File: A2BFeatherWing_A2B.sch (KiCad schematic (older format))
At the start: 13 parts, among them U2 AD2428W

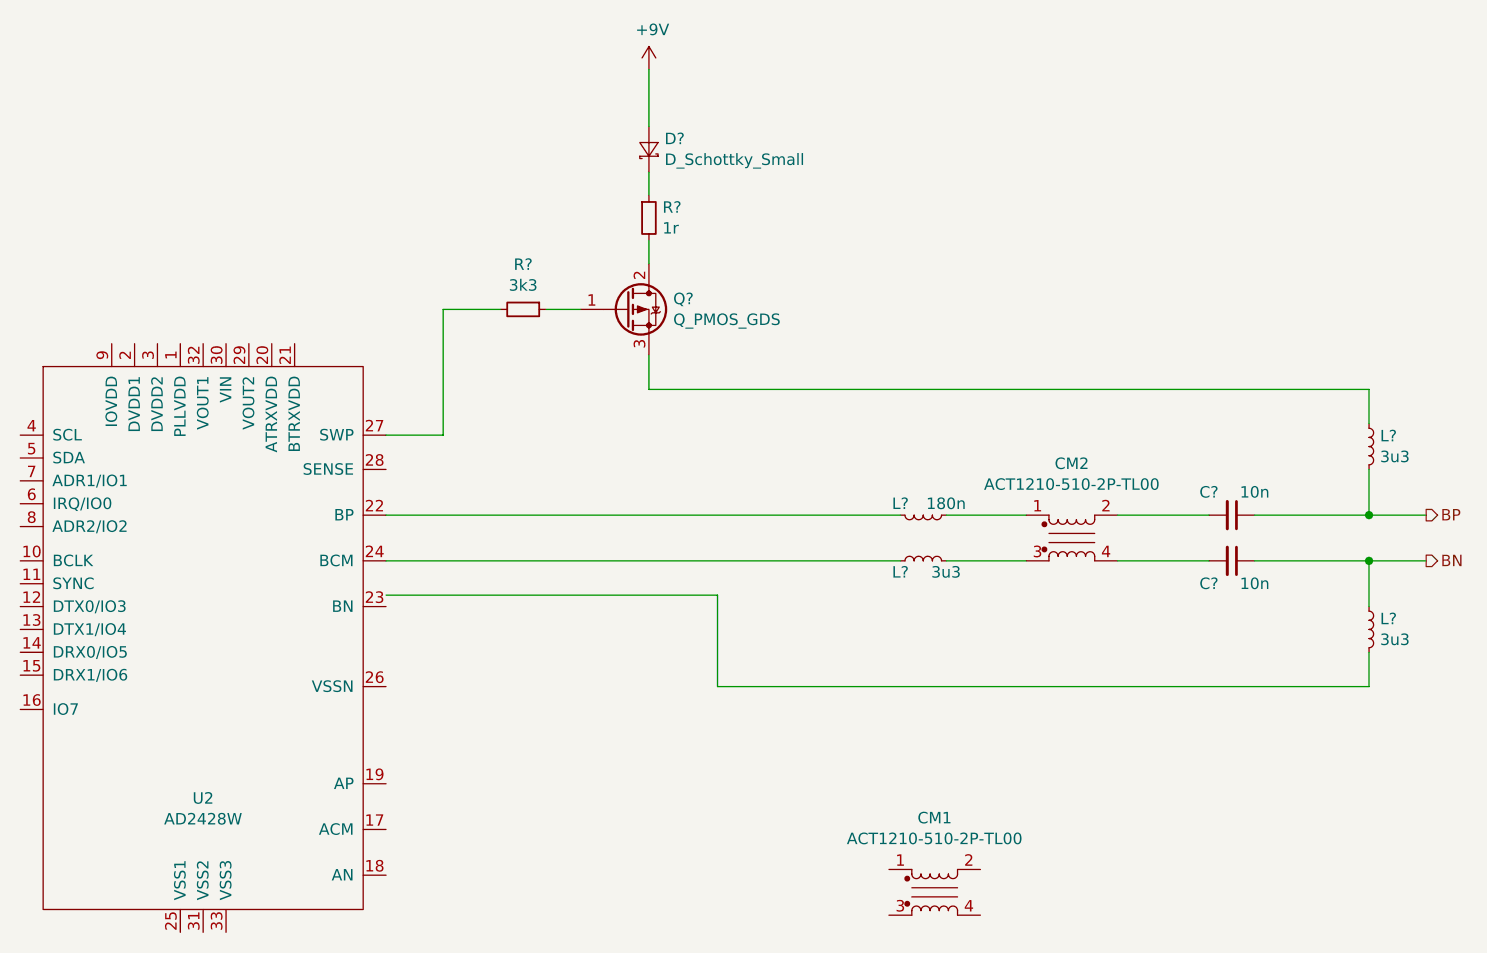
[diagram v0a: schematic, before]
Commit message: generate BOM, update some footprints
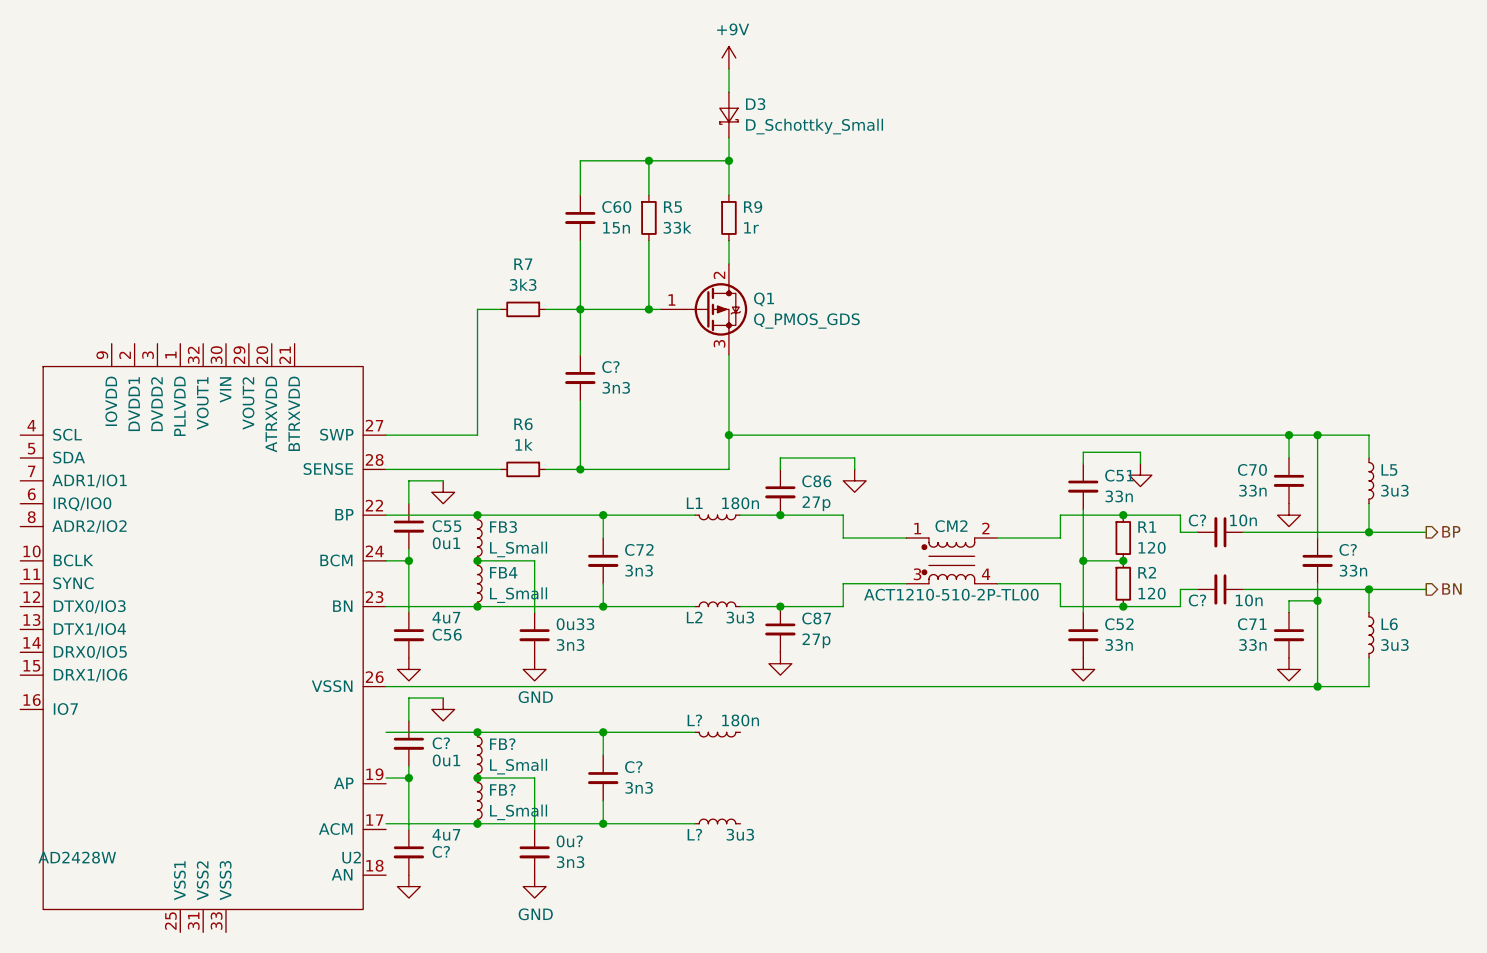
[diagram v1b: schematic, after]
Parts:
- removed CM1: ACT1210-510-2P-TL00, Knochi_Filters:CommonModeChoke_TDK_ACT1210, symbol Knochi_Inductors:ACT1210-510-2P-TL00
- added 0u33, 0u?, C72, C? (x2): 3n3, symbol Device:C_Small
- added C51, C52, C70, C71, C?: 33n, symbol Device:C_Small
- added C55, C?: 0u1, symbol Device:C_Small
- added C56, C?: 4u7, symbol Device:C_Small
- added C60: 15n, symbol Device:C_Small
- added C86, C87: 27p, symbol Device:C_Small
- added FB3, FB4, FB? (x2): L_Small, symbol Device:L_Small
- added L?: 180n, symbol Device:L_Small
- added L?: 3u3, symbol Device:L_Small
- added R1, R2: 120, symbol Device:R_Small
- added R5: 33k, symbol Device:R_Small
- added R6: 1k, symbol Device:R_Small
- gave numbers to parts that had none: 8
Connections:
- net labels added: GND
- wire segments 26 -> 101
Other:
- moved on the sheet: C?, CM2, D3, L1, L2, L5, L6, Q1, R9

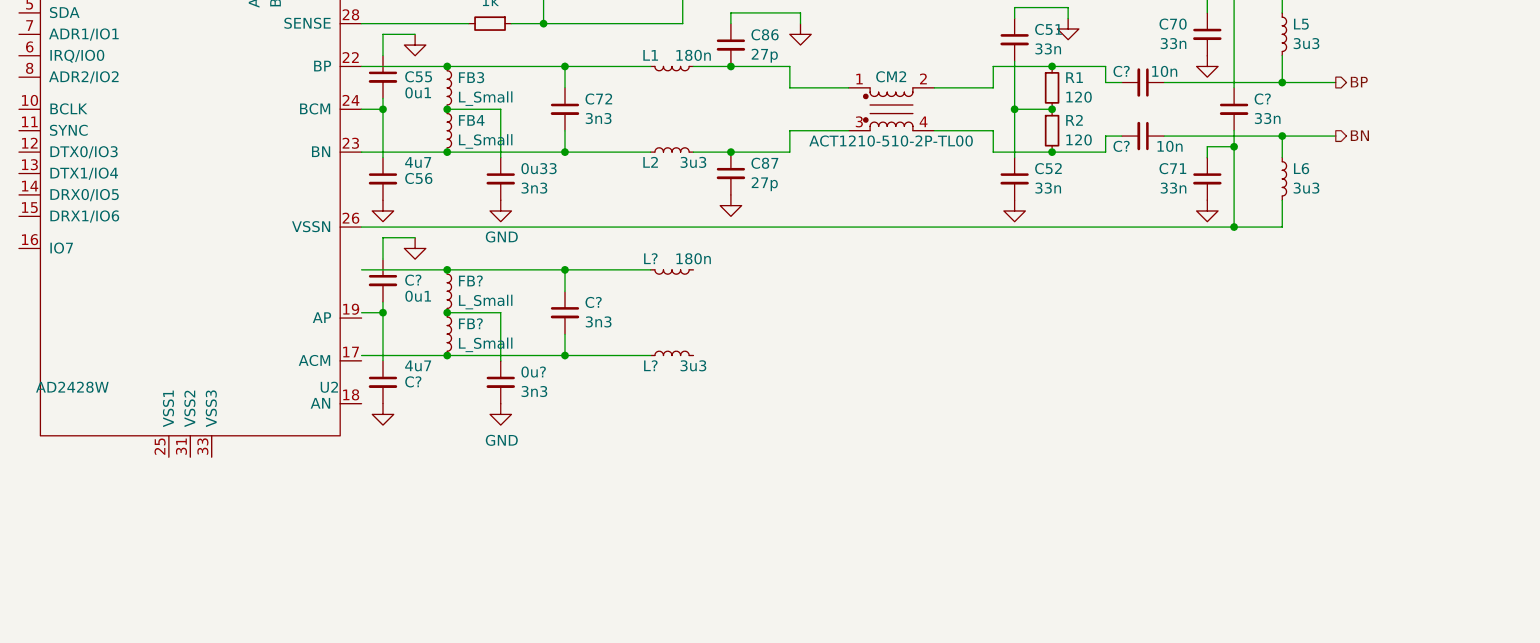
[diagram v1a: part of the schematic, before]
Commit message: local powered slave filtnet
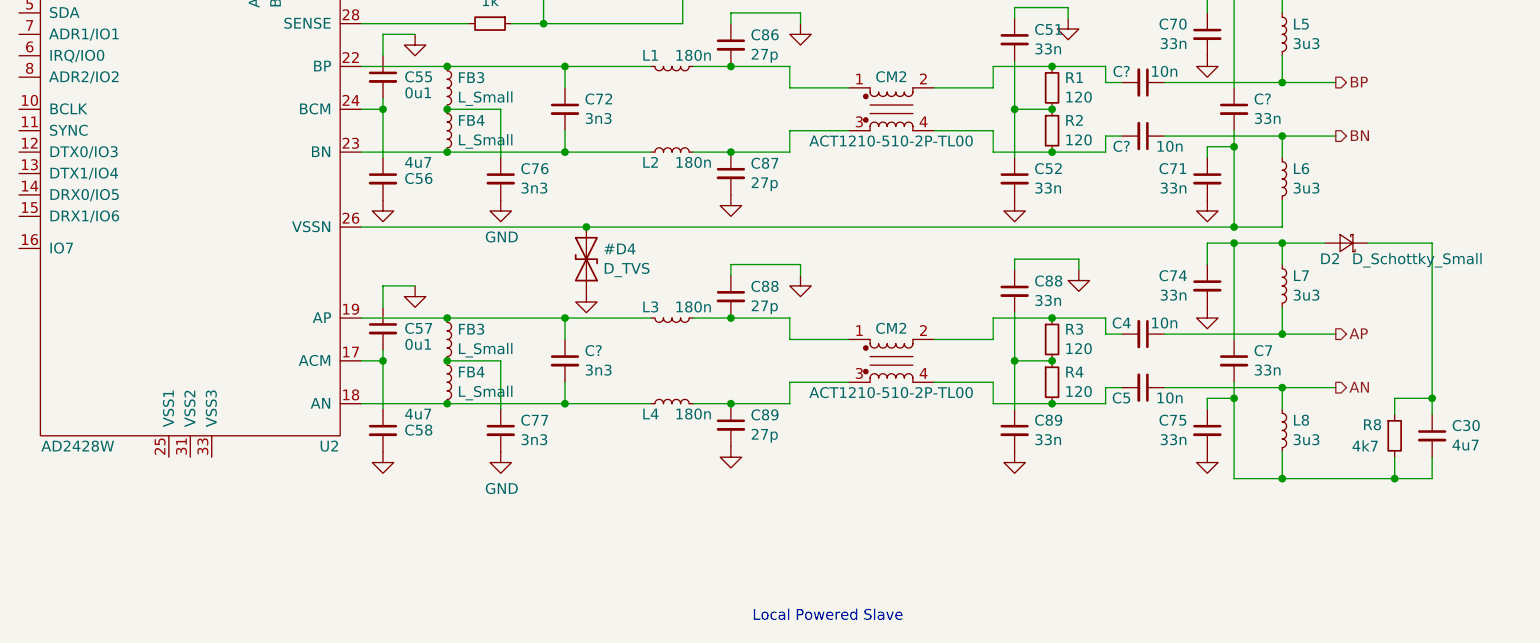
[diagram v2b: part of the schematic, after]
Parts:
- added C30: 4u7, symbol Device:C_Small
- added C4, C5: 10n, symbol Device:C_Small
- added C7, C74, C75, C88, C89: 33n, symbol Device:C_Small
- added C88, C89: 27p, symbol Device:C_Small
- added CM2: ACT1210-510-2P-TL00, Knochi_Filters:CommonModeChoke_TDK_ACT1210, symbol Knochi_Inductors:ACT1210-510-2P-TL00
- added D2: D_Schottky_Small, symbol Device:D_Schottky_Small
- added L7, L8: 3u3, symbol Device:L_Small
- added R3, R4: 120, symbol Device:R_Small
- added R8: 4k7, symbol Device:R_Small
- L2: value 3u3 -> 180n
- L4: renamed from L?; value 3u3 -> 180n
- gave numbers to parts that had none: 6
- renumbered 0u33 to C76
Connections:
- net labels added: AN, AP, D_TVS
- wire segments 101 -> 158
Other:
- note added: "Local Powered Slave"
- moved on the sheet: C57, C58, C77, C?, FB3, FB4, L3, L4

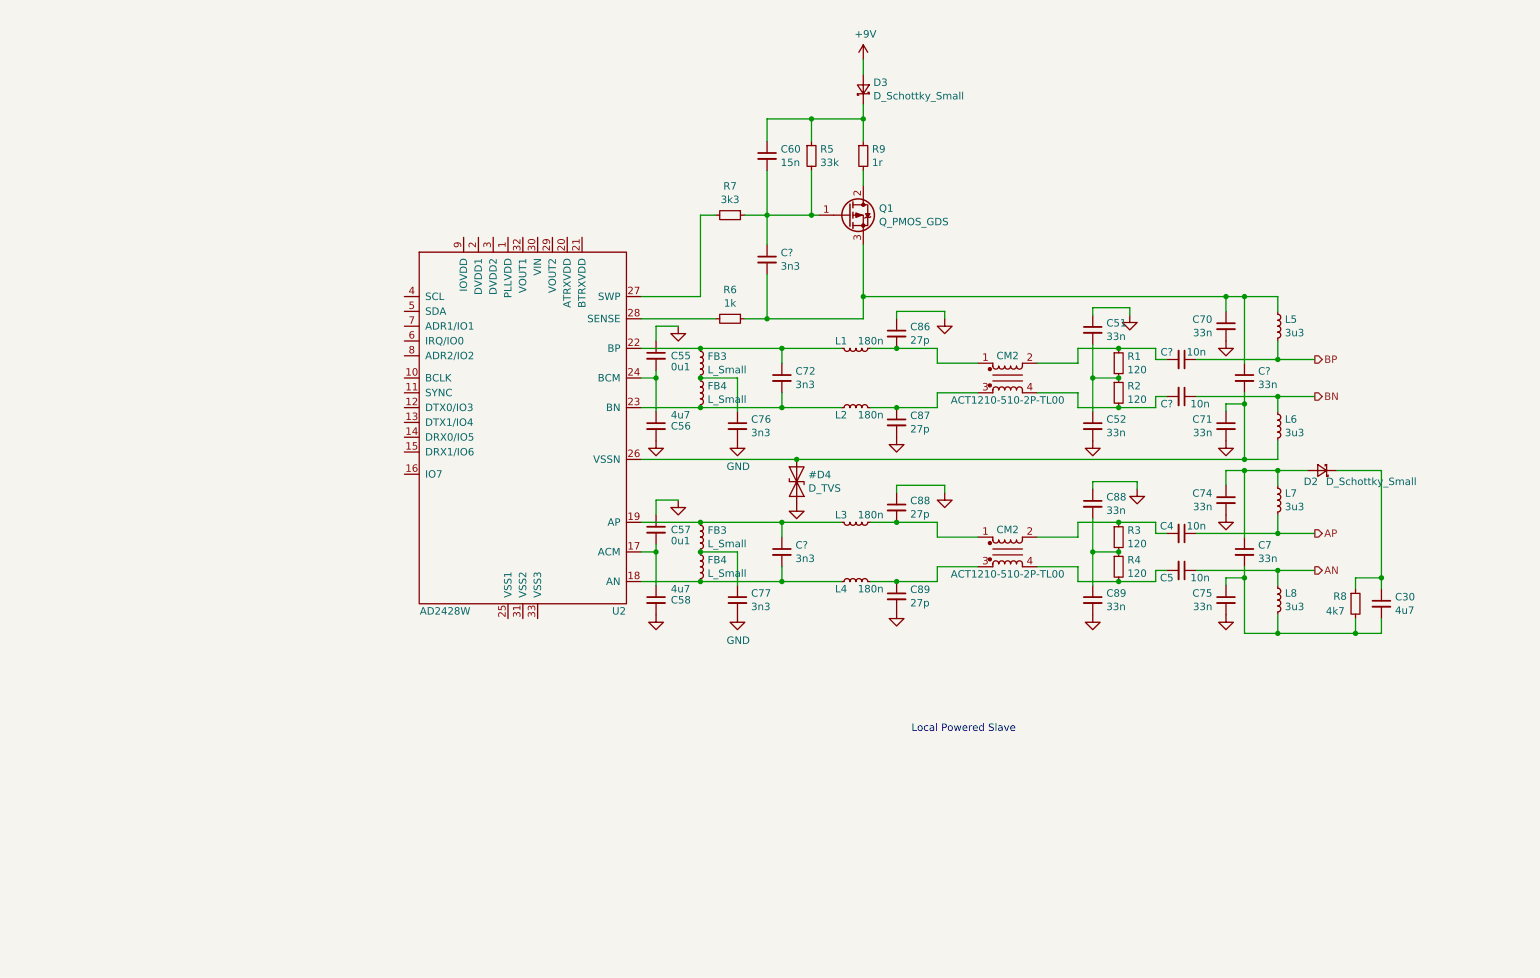
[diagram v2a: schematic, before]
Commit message: added datasheets, power
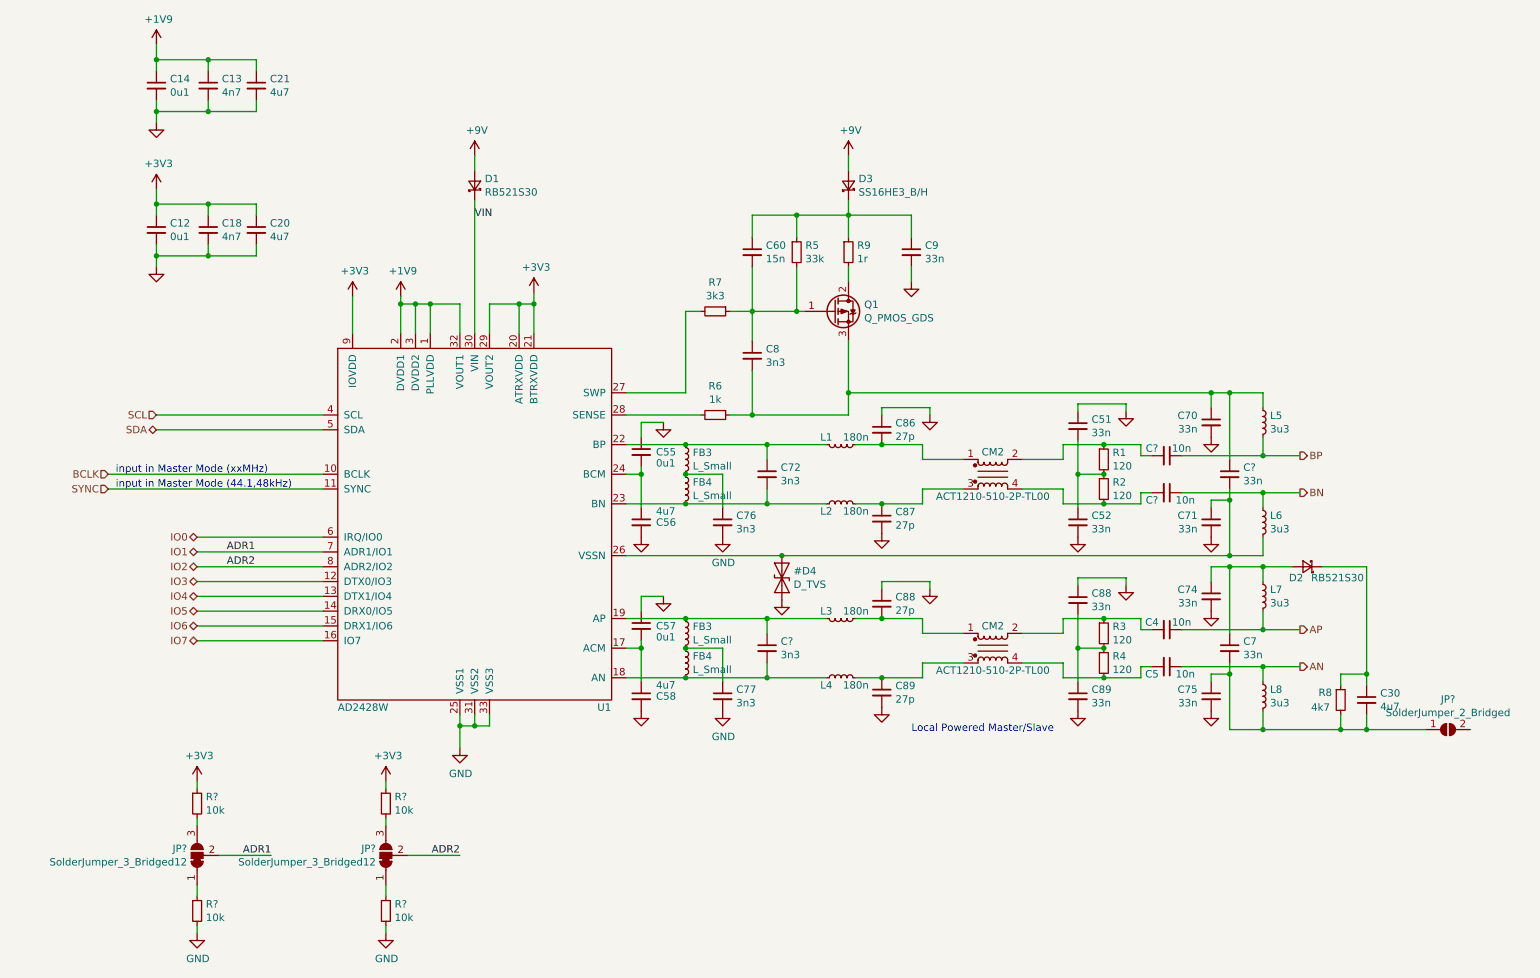
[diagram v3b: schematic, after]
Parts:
- removed U2: AD2428W, Package_DFN_QFN:QFN-32-1EP_5x5mm_P0.5mm_EP3.6x3.6mm, symbol Knochi_Transceivers:AD2428W
- added C12, C14: 0u1, symbol Device:C_Small
- added C13, C18: 4n7, symbol Device:C_Small
- added C20, C21: 4u7, symbol Device:C_Small
- added C9: 33n, symbol Device:C_Small
- added D1: RB521S30, symbol Device:D_Schottky_Small
- added JP?: SolderJumper_2_Bridged, symbol Jumper:SolderJumper_2_Open
- added JP? (x2): SolderJumper_3_Bridged12, symbol Jumper:SolderJumper_3_Bridged12
- added R? (x4): 10k, symbol Device:R_Small
- added U1: AD2428W, Package_DFN_QFN:QFN-32-1EP_5x5mm_P0.5mm_EP3.6x3.6mm, symbol A2BFeatherWing:AD2428W-Knochi_Transceivers
- D2: value D_Schottky_Small -> RB521S30
- D3: value D_Schottky_Small -> SS16HE3_B/H
- gave numbers to parts that had none: 1
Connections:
- net +9V: now also D1.2 (A)
- net GND: now also C12.2, C13.2, C14.2, C18.2, C20.2, C21.2, C9.2, R?.2, R?.2, U1.25 (VSS1), U1.31 (VSS2), U1.33 (VSS3)
- net at C57.2, C58.1: now also U1.17 (ACM)
- net at C?.2, FB4.2, L4.1: now also U1.18 (AN)
- net at C?.1, FB3.1, L3.2: now also U1.19 (AP)
- net at C72.1, FB3.1, L1.2: now also U1.22 (BP)
- net at C72.2, FB4.2, L2.1: now also U1.23 (BN)
- net at C55.2, C56.1: now also U1.24 (BCM)
- net at C71.1, C?.2, L6.2: now also U1.26 (VSSN)
- net at R7.2: now also U1.27 (SWP)
- net at R6.2: now also U1.28 (SENSE)
- net at C60.1, D3.1 (K), R5.1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: now also C9.1
- net at C30.2, C7.2, C75.1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: now also JP?.1 (A)
- new net: JP?.1 (A), R?.1 (x2)
- new net: JP?.3 (B), R?.2 (x2)
- new net +1V9: C13.1, C14.1, C21.1, U1.1 (PLLVDD), U1.2 (DVDD1), U1.3 (DVDD2), U1.32 (VOUT1)
- new net +3V3: C12.1, C18.1, C20.1, R?.1, R?.1, U1.20 (ATRXVDD), U1.21 (BTRXVDD), U1.29 (VOUT2), U1.9 (IOVDD)
- new net BCLK: U1.10 (BCLK)
- new net IO0: U1.6 (IRQ/IO0)
- new net IO1: JP?.2 (C), U1.7 (ADR1/IO1)
- new net IO2: JP?.2 (C), U1.8 (ADR2/IO2)
- new net IO3: U1.12 (DTX0/IO3)
- new net IO4: U1.13 (DTX1/IO4)
- new net IO5: U1.14 (DRX0/IO5)
- new net IO6: U1.15 (DRX1/IO6)
- new net IO7: U1.16 (IO7)
- new net SCL: U1.4 (SCL)
- new net SDA: U1.5 (SDA)
- new net SYNC: U1.11 (SYNC)
- new net VIN: D1.1 (K), U1.30 (VIN)
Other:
- note added: "Local Powered Master/Slave"
- note added: "input in Master Mode (44.1,48kHz)"
- note added: "input in Master Mode (xxMHz)"
- note removed: "Local Powered Slave"
- moved on the sheet: C30, C4, C5, C51, C52, C55, C56, C57, C58, C60, C7, C70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
